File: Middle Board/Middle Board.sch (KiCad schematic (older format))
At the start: 61 parts, among them J1 JTAG Connector, J2 Conn_Coaxial, J3 Conn_Coaxial, J4 Conn_Coaxial, J5 Conn_Coaxial, J6 Conn_02x10_Counter_Clockwise, SW1 SW_SPST, U1 ATSAMG55, U2 BNO055_Breakout, U3 MS5803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

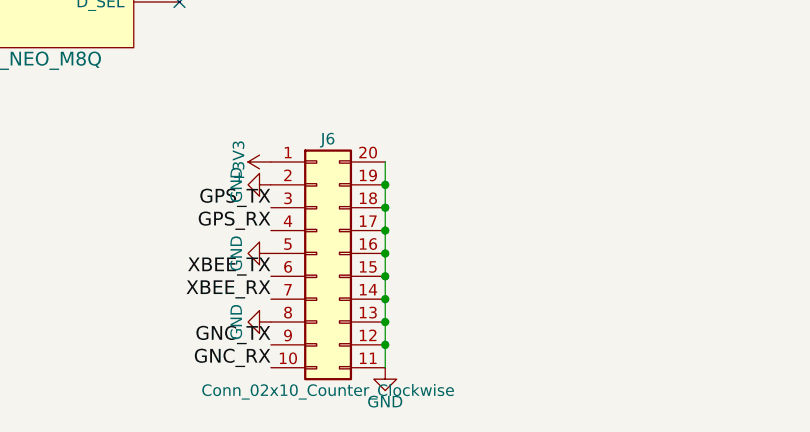
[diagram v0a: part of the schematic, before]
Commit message: Added some footprints
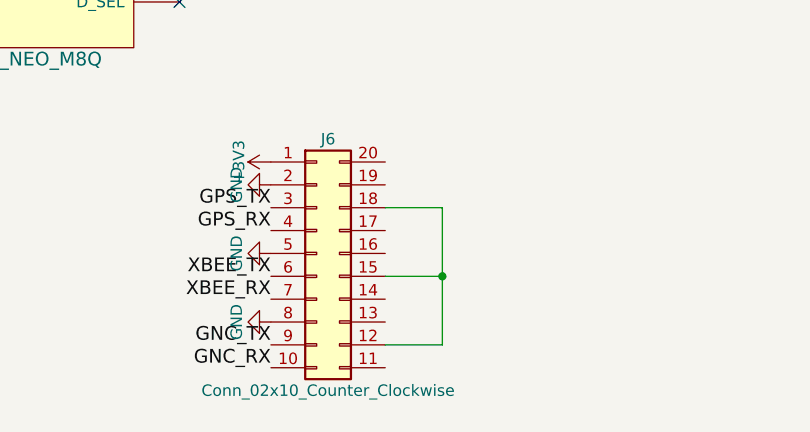
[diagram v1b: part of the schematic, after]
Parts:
- BT1: footprint (none) -> Battery_Holders:Keystone_3000_1x12mm-CoinCell; Digikey Part Number BK-885-CT-ND -> 36-3000-ND
- C1, C10, C12, C13, C14, C15, C2, C3, C4, C5, C6, C7, C8, C9: footprint (none) -> Capacitors_SMD:C_0603
- C11: footprint (none) -> Capacitors_SMD:C_0805
- D1, D2, D3, D4, D5, D6, D7: footprint (none) -> LEDs:LED_0603_HandSoldering
- R1, R10, R11, R12, R13, R14, R15, R16, R17, R18, R19, R2, R20, R21, R22, R23, R3, R4, R5, R6, R7, R8, R9: footprint (none) -> Resistors_SMD:R_0603
- U1: footprint (none) -> Housings_QFP:LQFP-64_10x10mm_Pitch0.5mm
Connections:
- net GND: no longer J6.11 (Pin_11), J6.12 (Pin_12), J6.13 (Pin_13), J6.14 (Pin_14), J6.15 (Pin_15), J6.16 (Pin_16), J6.17 (Pin_17), J6.18 (Pin_18), J6.19 (Pin_19), J6.20 (Pin_20)
- new net: J6.12 (Pin_12), J6.15 (Pin_15), J6.18 (Pin_18)

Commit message: More Middle Board Footprints
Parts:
- FL1: footprint (none) -> Custom Footprints:B39162B3520U410
- J1: footprint (none) -> Custom Footprints:10_pin_Cortex-M_connector
- J2, J3, J4, J5: footprint (none) -> Custom Footprints:SMA_SMD_RIGHT_ANGLE
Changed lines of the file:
@@
 F 0 "J1" H 4400 11350 50  0000 C CNN
 F 1 "JTAG Connector" H 4400 10750 50  0000 C CNN
-F 2 "" H 4350 11050 50  0001 C CNN
+F 2 "Custom Footprints:10_pin_Cortex-M_connector" H 4350 11050 50  0001 C CNN
 F 3 "" H 4350 11050 50  0001 C CNN
 F 4 "SAM8799-ND" H 4350 11050 60  0001 C CNN "Digikey Part Number"
@@
 F 0 "J2" H 8760 15020 50  0000 C CNN
 F 1 "Conn_Coaxial" V 8865 14900 50  0000 C CNN
-F 2 "" H 8750 14900 50  0001 C CNN
+F 2 "Custom Footprints:SMA_SMD_RIGHT_ANGLE" H 8750 14900 50  0001 C CNN
 F 3 "" H 8750 14900 50  0001 C CNN
 F 4 "931-1175-ND" H 8750 14900 60  0001 C CNN "Digikey Part Number"
@@
 F 0 "J3" H 8760 15620 50  0000 C CNN
 F 1 "Conn_Coaxial" V 8865 15500 50  0000 C CNN
-F 2 "" H 8750 15500 50  0001 C CNN
+F 2 "Custom Footprints:SMA_SMD_RIGHT_ANGLE" H 8750 15500 50  0001 C CNN
 F 3 "" H 8750 15500 50  0001 C CNN
 F 4 "931-1175-ND" H 8750 15500 60  0001 C CNN "Digikey Part Number"
@@
 F 0 "J4" H 8160 17970 50  0000 C CNN
 F 1 "Conn_Coaxial" V 8265 17850 50  0000 C CNN
-F 2 "" H 8150 17850 50  0001 C CNN
+F 2 "Custom Footprints:SMA_SMD_RIGHT_ANGLE" H 8150 17850 50  0001 C CNN
 F 3 "" H 8150 17850 50  0001 C CNN
 F 4 "931-1175-ND" H 8150 17850 60  0001 C CNN "Digikey Part Number"
@@
 F 0 "J5" H 8160 18570 50  0000 C CNN
 F 1 "Conn_Coaxial" V 8265 18450 50  0000 C CNN
-F 2 "" H 8150 18450 50  0001 C CNN
+F 2 "Custom Footprints:SMA_SMD_RIGHT_ANGLE" H 8150 18450 50  0001 C CNN
 F 3 "" H 8150 18450 50  0001 C CNN
 F 4 "931-1175-ND" H 8150 18450 60  0001 C CNN "Digikey Part Number"
@@
 F 0 "FL1" H 5200 18750 60  0000 C CNN
 F 1 "B39162B3520U410" H 5200 18650 60  0000 C CNN
-F 2 "" H 5200 18300 60  0001 C CNN
+F 2 "Custom Footprints:B39162B3520U410" H 5200 18300 60  0001 C CNN
 F 3 "" H 5200 18300 60  0001 C CNN
 F 4 "495-2363-6-ND" H 5200 18300 60  0001 C CNN "Digikey Part Number"

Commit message: Finished middle board footprints
PCB Time!
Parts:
- J6: footprint (none) -> Custom Footprints:CONN_CARD_02x10_MALE
- SW1: footprint (none) -> Custom Footprints:SW_SPST_SMD
- U2: footprint (none) -> Custom Footprints:BNO055_Breakout
- U3: footprint (none) -> Custom Footprints:MS5803
- U4, U6: footprint (none) -> Custom Footprints:SMD_PD_ANAREN
- U5: footprint (none) -> Custom Footprints:XBEE_PRO_SX; Digikey Part Number 602-2007-ND -> 602-1889-ND
- U7: footprint (none) -> Custom Footprints:UBX_NEO_M8Q
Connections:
- net +3V3: now also U3.5 (VDD)
- net BNO055_RST: now also U1.12 (PA8); no longer U1.44 (PA11)
- net GND: now also C13.1, J6.12 (Pin_12), J6.15 (Pin_15), J6.18 (Pin_18), U3.6 (PS); no longer C13.2, U3.3 (CSB)
- net SCL: no longer U3.1 (SCLK)
- net SDA: no longer U3.7 (SDI/SDA)
- net SCLK: now reaches U1.41 (PA14)
- net SCLK: now also U3.1 (SCLK)
- net MOSI: now reaches U1.42 (PA13)
- net MOSI: now also U3.7 (SDI/SDA)
- net MISO: now reaches U1.43 (PA12)
- net MISO: now also U3.8 (SDO)
- new net MS5803_CS: U1.44 (PA11), U3.3 (CSB)
- no-connect marks 34 -> 33
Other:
- moved on the sheet: C13
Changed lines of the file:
@@
 F 0 "U2" H 5000 12850 60  0000 C CNN
 F 1 "BNO055_Breakout" H 5000 12150 60  0000 C CNN
-F 2 "" H 5000 12150 60  0001 C CNN
+F 2 "Custom Footprints:BNO055_Breakout" H 5000 12150 60  0001 C CNN
 F 3 "" H 5000 12150 60  0001 C CNN
 F 4 "1528-1426-ND" H 5000 12950 50  0001 C CNN "Digikey Part Number"
@@
 F 0 "SW1" H 4150 9425 50  0000 C CNN
 F 1 "SW_SPST" H 4150 9200 50  0000 C CNN
-F 2 "" H 4150 9300 50  0001 C CNN
+F 2 "Custom Footprints:SW_SPST_SMD" H 4150 9300 50  0001 C CNN
 F 3 "" H 4150 9300 50  0001 C CNN
 F 4 "CKN9112CT-ND" H 4150 9525 50  0001 C CNN "Digikey Part Number"
@@
 L C_Small C13
 U 1 1 5A6EB0CF
-P 4900 14450
-F 0 "C13" H 4910 14520 50  0000 L CNN
-F 1 "100 nF" H 4910 14370 50  0000 L CNN
-F 2 "Capacitors_SMD:C_0603" H 4900 14450 50  0001 C CNN
-F 3 "" H 4900 14450 50  0001 C CNN
-F 4 "490-1532-1-ND" H 4900 14450 60  0001 C CNN "Digikey Part Number"
-	1    4900 14450
-	0    1    1    0
+P 5850 14150
+F 0 "C13" H 5860 14220 50  0000 L CNN
+F 1 "100 nF" H 5860 14070 50  0000 L CNN
+F 2 "Capacitors_SMD:C_0603" H 5850 14150 50  0001 C CNN
+F 3 "" H 5850 14150 50  0001 C CNN
+F 4 "490-1532-1-ND" H 5850 14150 60  0001 C CNN "Digikey Part Number"
+	1    5850 14150
+	-1   0    0    1
 $EndComp
 $Comp
 L +3V3 #PWR011
 U 1 1 5A6EB659
-P 5400 14450
-F 0 "#PWR011" H 5400 14300 50  0001 C CNN
-F 1 "+3V3" H 5400 14590 50  0000 C CNN
-F 2 "" H 5400 14450 50  0001 C CNN
-F 3 "" H 5400 14450 50  0001 C CNN
-	1    5400 14450
+P 6150 14050
+F 0 "#PWR011" H 6150 13900 50  0001 C CNN
+F 1 "+3V3" H 6150 14190 50  0000 C CNN
+F 2 "" H 6150 14050 50  0001 C CNN
+F 3 "" H 6150 14050 50  0001 C CNN
+	1    6150 14050
 	1    0    0    -1
 $EndComp
@@
 F 0 "U5" H 3950 16500 60  0000 C CNN
 F 1 "XBee_PRO_SX" H 5850 15000 60  0000 C CNN
-F 2 "" H 3950 16500 60  0001 C CNN
+F 2 "Custom Footprints:XBEE_PRO_SX" H 3950 16500 60  0001 C CNN
 F 3 "" H 3950 16500 60  0001 C CNN
-F 4 "602-2007-ND" H 3950 16600 50  0001 C CNN "Digikey Part Number"
+F 4 "602-1889-ND" H 3950 16600 50  0001 C CNN "Digikey Part Number"
 	1    4950 15800
 	1    0    0    -1
@@
 F 0 "U4" H 7500 15700 60  0000 C CNN
 F 1 "PD0810J5050S2HF" H 7500 14900 60  0000 C CNN
-F 2 "" H 7500 15700 60  0001 C CNN
+F 2 "Custom Footprints:SMD_PD_ANAREN" H 7500 15700 60  0001 C CNN
 F 3 "" H 7500 15700 60  0001 C CNN
 F 4 "1173-1093-1-ND" H 7500 15800 50  0001 C CNN "Digikey Part Number"
@@
 F 0 "U3" H 4850 14500 60  0000 C CNN
 F 1 "MS5803" H 4850 13900 60  0000 C CNN
-F 2 "" H 4850 14500 60  0001 C CNN
+F 2 "Custom Footprints:MS5803" H 4850 14500 60  0001 C CNN
 F 3 "" H 4850 14500 60  0001 C CNN
 F 4 "223-1623-5-ND" H 4850 14600 50  0001 C CNN "Digikey Part Number"
@@
 F 0 "U6" H 6900 18650 60  0000 C CNN
 F 1 "PD0922J5050S2HF" H 6900 17850 60  0000 C CNN
-F 2 "" H 6900 18650 60  0001 C CNN
+F 2 "Custom Footprints:SMD_PD_ANAREN" H 6900 18650 60  0001 C CNN
 F 3 "" H 6900 18650 60  0001 C CNN
 F 4 "1173-1094-1-ND" H 6900 18750 50  0001 C CNN "Digikey Part Number"
@@
 F 0 "U7" H 3350 19400 60  0000 C CNN
 F 1 "UBX_NEO_M8Q" H 3350 18000 60  0000 C CNN
-F 2 "" H 3350 19300 60  0001 C CNN
+F 2 "Custom Footprints:UBX_NEO_M8Q" H 3350 19300 60  0001 C CNN
 F 3 "" H 3350 19300 60  0001 C CNN
 F 4 "672-1009-1-ND" H 3350 19500 50  0001 C CNN "Digikey Part Number"
@@
 L GND #PWR042
 U 1 1 5A716165
-P 4150 14450
-F 0 "#PWR042" H 4150 14200 50  0001 C CNN
-F 1 "GND" H 4150 14300 50  0000 C CNN
-F 2 "" H 4150 14450 50  0001 C CNN
-F 3 "" H 4150 14450 50  0001 C CNN
-	1    4150 14450
+P 5850 14250
+F 0 "#PWR042" H 5850 14000 50  0001 C CNN
+F 1 "GND" H 5850 14100 50  0000 C CNN
+F 2 "" H 5850 14250 50  0001 C CNN
+F 3 "" H 5850 14250 50  0001 C CNN
+	1    5850 14250
 	1    0    0    -1
 $EndComp
@@
 F 0 "J6" H 4650 20750 50  0000 C CNN
 F 1 "Conn_02x10_Counter_Clockwise" H 4650 19650 50  0000 C CNN
-F 2 "" H 4600 20250 50  0001 C CNN
+F 2 "Custom Footprints:CONN_CARD_02x10_MALE" H 4600 20250 50  0001 C CNN
 F 3 "" H 4600 20250 50  0001 C CNN
 F 4 "S3299-ND" H 4600 20250 60  0001 C CNN "Digikey Part Number"
@@
 Text Label 3250 5300 2    60   ~ 0
 TDI
-Text Label 6400 4400 0    60   ~ 0
+Text Label 6400 4100 0    60   ~ 0
 BNO055_RST
 Text Label 6400 4300 0    60   ~ 0
@@
 nRST
 Text Label 4150 13800 2    60   ~ 0
-SCL
+SCLK
 Text Label 5600 13850 0    60   ~ 0
-SDA
+MOSI
 Text Label 6300 15300 0    60   ~ 0
 XBEE_RF_50Ω
@@
 NoConn ~ 5550 12550
 NoConn ~ 4450 12350
-NoConn ~ 5400 13750
 NoConn ~ 3650 15700
 NoConn ~ 3650 15800
@@
 NoConn ~ 4000 19050
 NoConn ~ 4000 19150
+$Comp
+L GND #PWR049
+U 1 1 5A715134
+P 5150 20650
+F 0 "#PWR049" H 5150 20400 50  0001 C CNN
+F 1 "GND" H 5150 20500 50  0000 C CNN
+F 2 "" H 5150 20650 50  0001 C CNN
+F 3 "" H 5150 20650 50  0001 C CNN
+	1    5150 20650
+	1    0    0    -1
+$EndComp
+Text Label 5600 13750 0    60   ~ 0
+MISO
+$Comp
+L GND #PWR050
+U 1 1 5A737E54
+P 5400 13950
+F 0 "#PWR050" H 5400 13700 50  0001 C CNN
+F 1 "GND" H 5400 13800 50  0000 C CNN
+F 2 "" H 5400 13950 50  0001 C CNN
+F 3 "" H 5400 13950 50  0001 C CNN
+	1    5400 13950
+	0    -1   -1   0
+$EndComp
+$Comp
+L GND #PWR051
+U 1 1 5A738741
+P 4300 13900
+F 0 "#PWR051" H 4300 13650 50  0001 C CNN
+F 1 "GND" H 4300 13750 50  0000 C CNN
+F 2 "" H 4300 13900 50  0001 C CNN
+F 3 "" H 4300 13900 50  0001 C CNN
+	1    4300 13900
+	0    1    1    0
+$EndComp
+Text Label 4150 14000 2    60   ~ 0
+MS5803_CS
 Wire Wire Line
 	4950 2950 5850 2950
@@
 Wire Wire Line
 	4150 13800 4300 13800
-Wire Wire Line
-	4300 13900 4150 13900
-Wire Wire Line
-	4150 13900 4150 14450
-Wire Wire Line
-	4150 14450 4800 14450
-Wire Wire Line
-	5600 14450 5000 14450
-Wire Wire Line
-	5600 13950 5600 14450
-Wire Wire Line
-	5600 14050 5400 14050
-Wire Wire Line
-	5400 13950 5600 13950
-Wire Wire Line
-	4300 14000 4150 14000
 Wire Wire Line
 	6050 4200 6400 4200
@@
 Connection ~ 4750 9100
 Connection ~ 4750 9500
-Connection ~ 5600 14050
-Connection ~ 4150 14000
 Connection ~ 5100 7750
 Connection ~ 4800 6850
@@
 	5150 20050 4900 20050
 Connection ~ 5150 20350
+Wire Wire Line
+	5600 13750 5400 13750
+Wire Wire Line
+	5400 14050 6150 14050
+Wire Wire Line
+	4150 14000 4300 14000
+Wire Wire Line
+	6050 4100 6400 4100
+Wire Wire Line
+	6050 4500 6400 4500
+Wire Wire Line
+	6400 4600 6050 4600
+Wire Wire Line
+	6400 4700 6050 4700
+Text Label 6400 4400 0    60   ~ 0
+MS5803_CS
+Text Label 6400 4500 0    60   ~ 0
+MISO
+Text Label 6400 4600 0    60   ~ 0
+MOSI
+Text Label 6400 4700 0    60   ~ 0
+SCLK
 $EndSCHEMATC

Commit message: Small Changes
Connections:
- net +3V3: now also J6.11 (Pin_11)
- net GNC_RX: now also J6.4 (Pin_4); no longer J6.10 (Pin_10)
- net GNC_TX: now also J6.3 (Pin_3); no longer J6.9 (Pin_9)
- net GND: now also J6.13 (Pin_13), J6.14 (Pin_14), J6.16 (Pin_16), J6.17 (Pin_17), J6.19 (Pin_19), J6.20 (Pin_20)
- net GPS_RX: now also J6.10 (Pin_10); no longer J6.4 (Pin_4)
- net GPS_TX: now also J6.9 (Pin_9); no longer J6.3 (Pin_3)
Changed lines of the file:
@@
 Text Label 2150 18950 2    60   ~ 0
 GPS_RX
-Text Label 4400 20050 2    60   ~ 0
+Text Label 4400 20650 2    60   ~ 0
 GPS_TX
-Text Label 4400 20150 2    60   ~ 0
+Text Label 4400 20750 2    60   ~ 0
 GPS_RX
 Text Label 4400 20350 2    60   ~ 0
@@
 Text Label 4400 20450 2    60   ~ 0
 XBEE_RX
-Text Label 4400 20750 2    60   ~ 0
+Text Label 4400 20150 2    60   ~ 0
 GNC_RX
-Text Label 4400 20650 2    60   ~ 0
+Text Label 4400 20050 2    60   ~ 0
 GNC_TX
 NoConn ~ 4150 11150
@@
 L GND #PWR049
 U 1 1 5A715134
-P 5150 20650
-F 0 "#PWR049" H 5150 20400 50  0001 C CNN
-F 1 "GND" H 5150 20500 50  0000 C CNN
-F 2 "" H 5150 20650 50  0001 C CNN
-F 3 "" H 5150 20650 50  0001 C CNN
-	1    5150 20650
+P 5150 19850
+F 0 "#PWR049" H 5150 19600 50  0001 C CNN
+F 1 "GND" H 5150 19700 50  0000 C CNN
+F 2 "" H 5150 19850 50  0001 C CNN
+F 3 "" H 5150 19850 50  0001 C CNN
+	1    5150 19850
 	1    0    0    -1
 $EndComp
@@
 Connection ~ 6950 15500
 Wire Wire Line
-	5150 20650 4900 20650
-Wire Wire Line
-	5150 20050 5150 20650
-Wire Wire Line
-	5150 20350 4900 20350
-Wire Wire Line
-	5150 20050 4900 20050
-Connection ~ 5150 20350
-Wire Wire Line
 	5600 13750 5400 13750
 Wire Wire Line
@@
 Text Label 6400 4700 0    60   ~ 0
 SCLK
+Wire Wire Line
+	4900 19850 5150 19850
+Connection ~ 4900 19850
+Connection ~ 4900 19950
+Connection ~ 4900 20050
+Connection ~ 4900 20150
+Connection ~ 4900 20250
+Connection ~ 4900 20350
+Connection ~ 4900 20450
+Connection ~ 4900 20550
+Connection ~ 4900 20650
+Wire Wire Line
+	4900 20650 4900 19850
+$Comp
+L +3V3 #PWR?
+U 1 1 5A81B3A7
+P 4900 20750
+F 0 "#PWR?" H 4900 20600 50  0001 C CNN
+F 1 "+3V3" H 4900 20890 50  0000 C CNN
+F 2 "" H 4900 20750 50  0001 C CNN
+F 3 "" H 4900 20750 50  0001 C CNN
+	1    4900 20750
+	0    1    1    0
+$EndComp
 $EndSCHEMATC

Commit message: A whole lot of changes
Kinda forgot what they all were
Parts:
- BT1: symbol Battery_Cell -> device:Battery_Cell
- C1, C10, C11, C12, C13, C14, C15, C2, C3, C4, C5, C6, C7, C8, C9: symbol C_Small -> device:C_Small
- D1, D2, D3, D4, D5, D6, D7: symbol LED -> device:LED
- FL1: symbol B39162B3520U410 -> Custom-Parts:B39162B3520U410
- J1: symbol Conn_02x05_Odd_Even -> Middle-Board-rescue:Conn_02x05_Odd_Even
- J2, J3, J4, J5: symbol Conn_Coaxial -> Middle-Board-rescue:Conn_Coaxial
- J6: symbol Conn_02x10_Counter_Clockwise -> Middle-Board-rescue:Conn_02x10_Counter_Clockwise
- R1, R10, R11, R12, R13, R14, R15, R16, R17, R18, R19, R2, R20, R21, R22, R23, R3, R4, R5, R6, R7, R8, R9: symbol R -> device:R
- SW1: symbol SW_SPST -> Middle-Board-rescue:SW_SPST
- U1: symbol ATSAMG55 -> Custom-Parts:ATSAMG55
- U2: symbol BNO055_Breakout -> Custom-Parts:BNO055_Breakout
- U3: symbol MS5803 -> Custom-Parts:MS5803
- U4: symbol PD0810J5050S2HF -> Custom-Parts:PD0810J5050S2HF
- U5: symbol XBee_PRO_SX -> Custom-Parts:XBee_PRO_SX
- U6: symbol PD0922J5050S2HF -> Custom-Parts:PD0922J5050S2HF
- U7: symbol UBX_NEO_M8Q -> Custom-Parts:UBX_NEO_M8Q
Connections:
- net +3V3: no longer J6.11 (Pin_11)
- net GND: no longer J6.12 (Pin_12), J6.13 (Pin_13), J6.14 (Pin_14), J6.15 (Pin_15), J6.16 (Pin_16), J6.17 (Pin_17), J6.18 (Pin_18), J6.19 (Pin_19), J6.20 (Pin_20)
